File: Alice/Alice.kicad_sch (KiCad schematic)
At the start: 46 parts

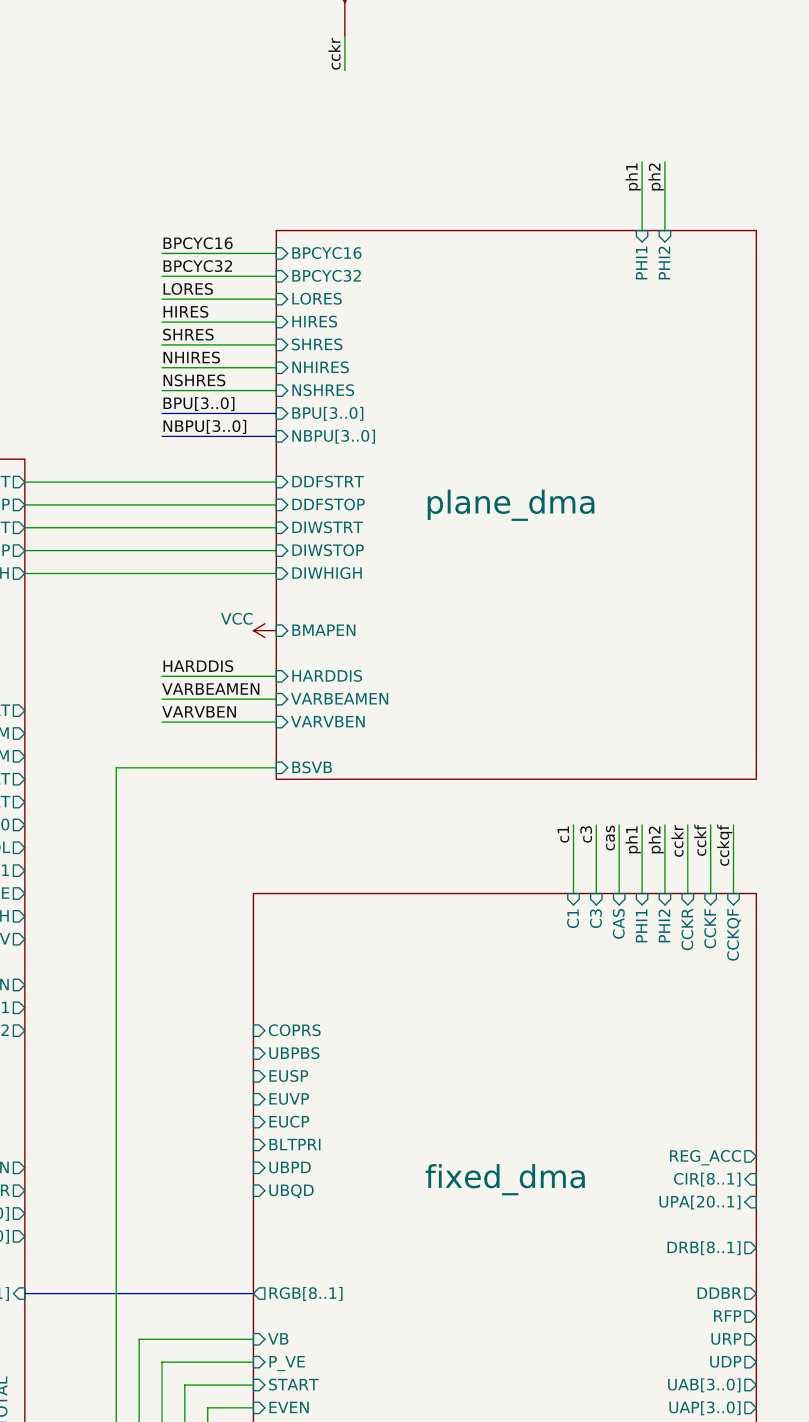
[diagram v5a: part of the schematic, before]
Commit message: Bitplane DMA runs in simulation
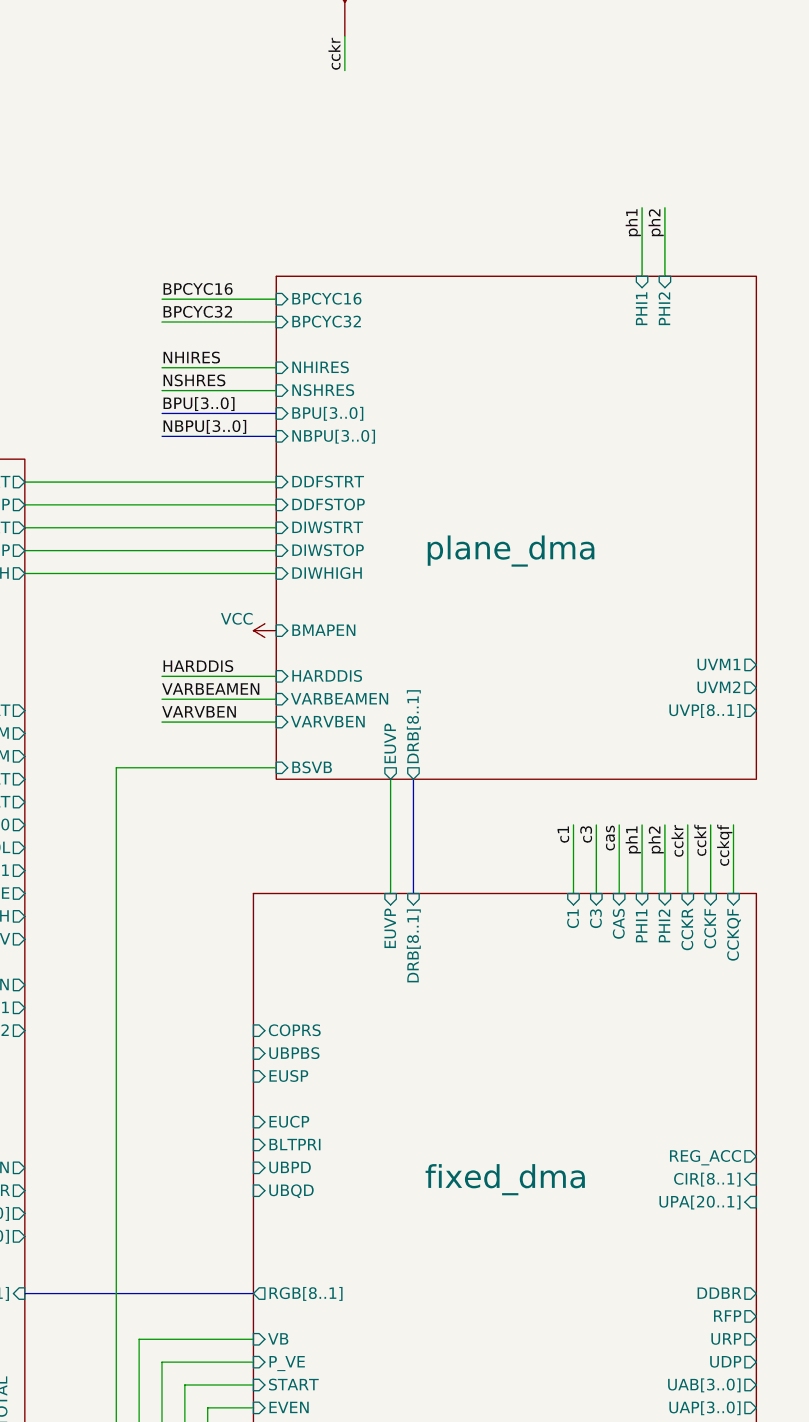
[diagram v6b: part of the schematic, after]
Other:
- sheet plane_dma ports: added DRB[8..1], EUVP, UVM1, UVM2, UVP[8..1]; removed HIRES, LORES, SHRES

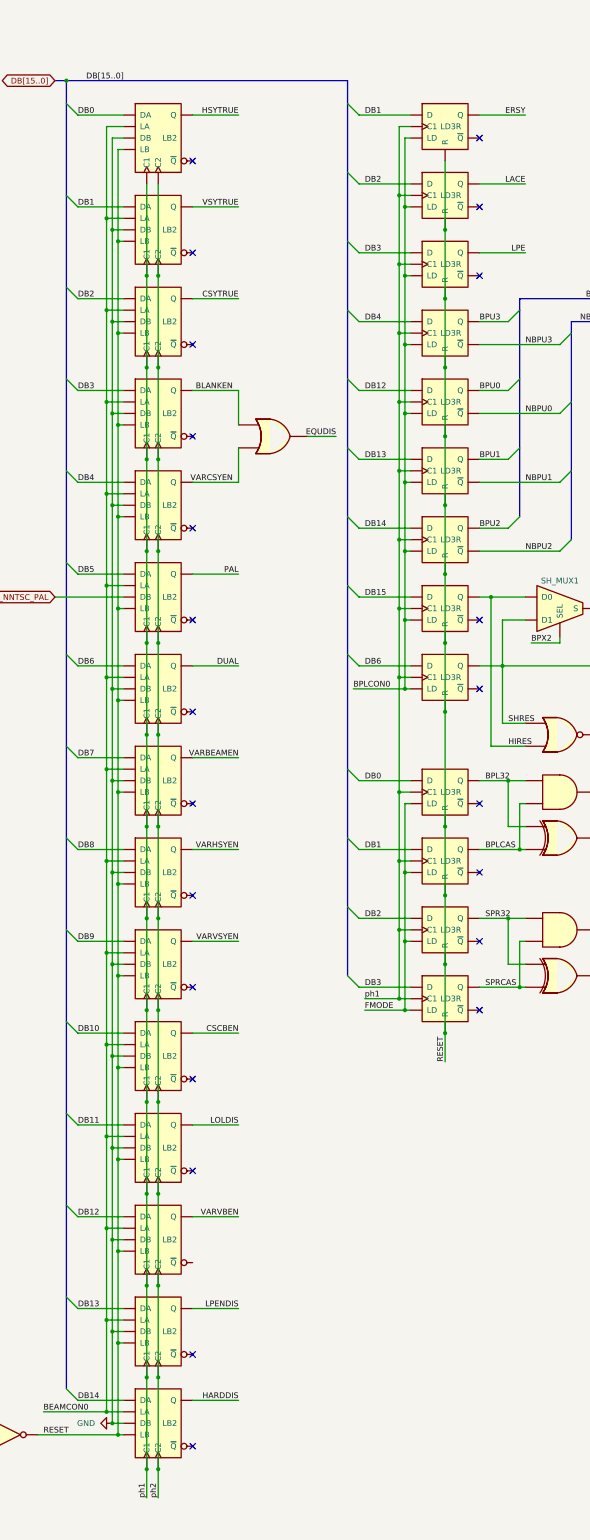
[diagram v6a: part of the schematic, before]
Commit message: Schematics have been annotated
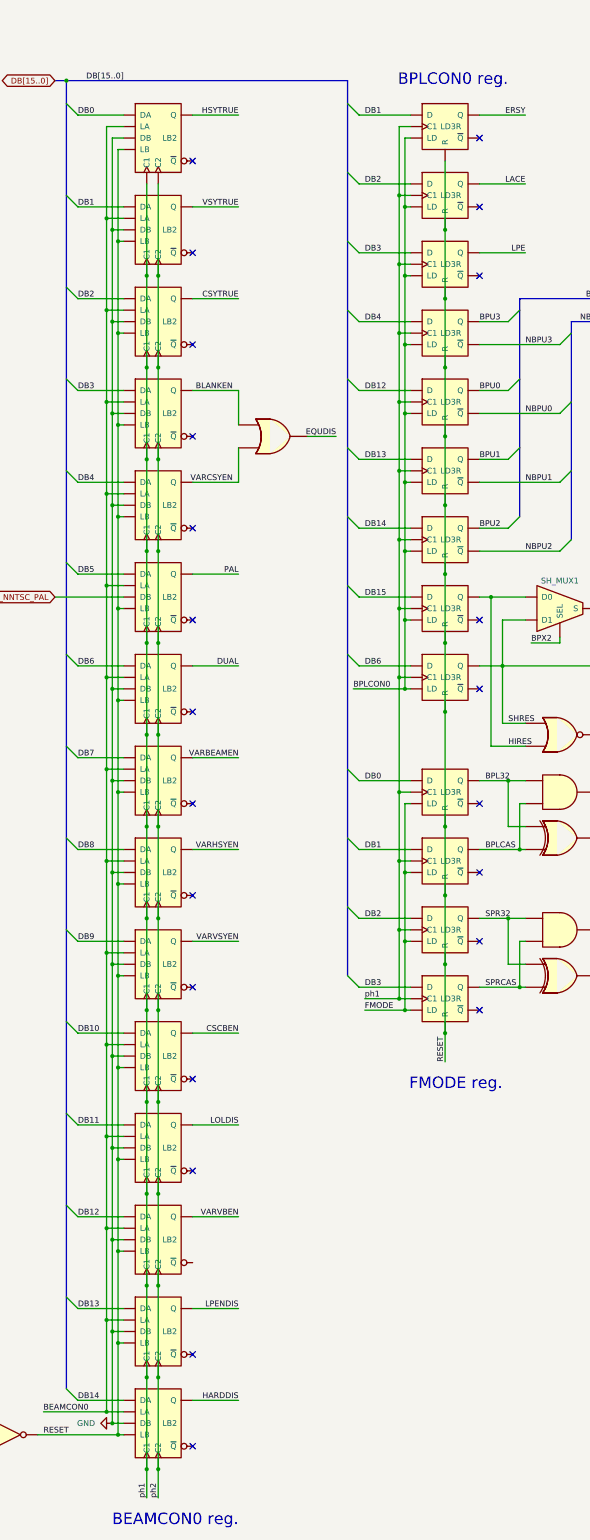
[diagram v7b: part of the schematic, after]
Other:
- note added: "BEAMCON0 reg."
- note added: "BPLCON0 reg."
- note added: "FMODE reg."
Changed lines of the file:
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@@
     (stroke (width 0) (type default) (color 0 0 0 0))
+  )
+  (text "FMODE reg." (at 147.32 287.02 180)
+    (effects (font (size 2.54 2.54)) (justify right bottom))
+  )
+  (text "BPLCON0 reg." (at 148.59 64.77 180)
+    (effects (font (size 2.54 2.54)) (justify right bottom))
+  )
+  (text "BEAMCON0 reg." (at 88.9 383.54 180)
+    (effects (font (size 2.54 2.54)) (justify right bottom))
   )
   (label "CSYTRUE" (at 88.9 111.76 180)

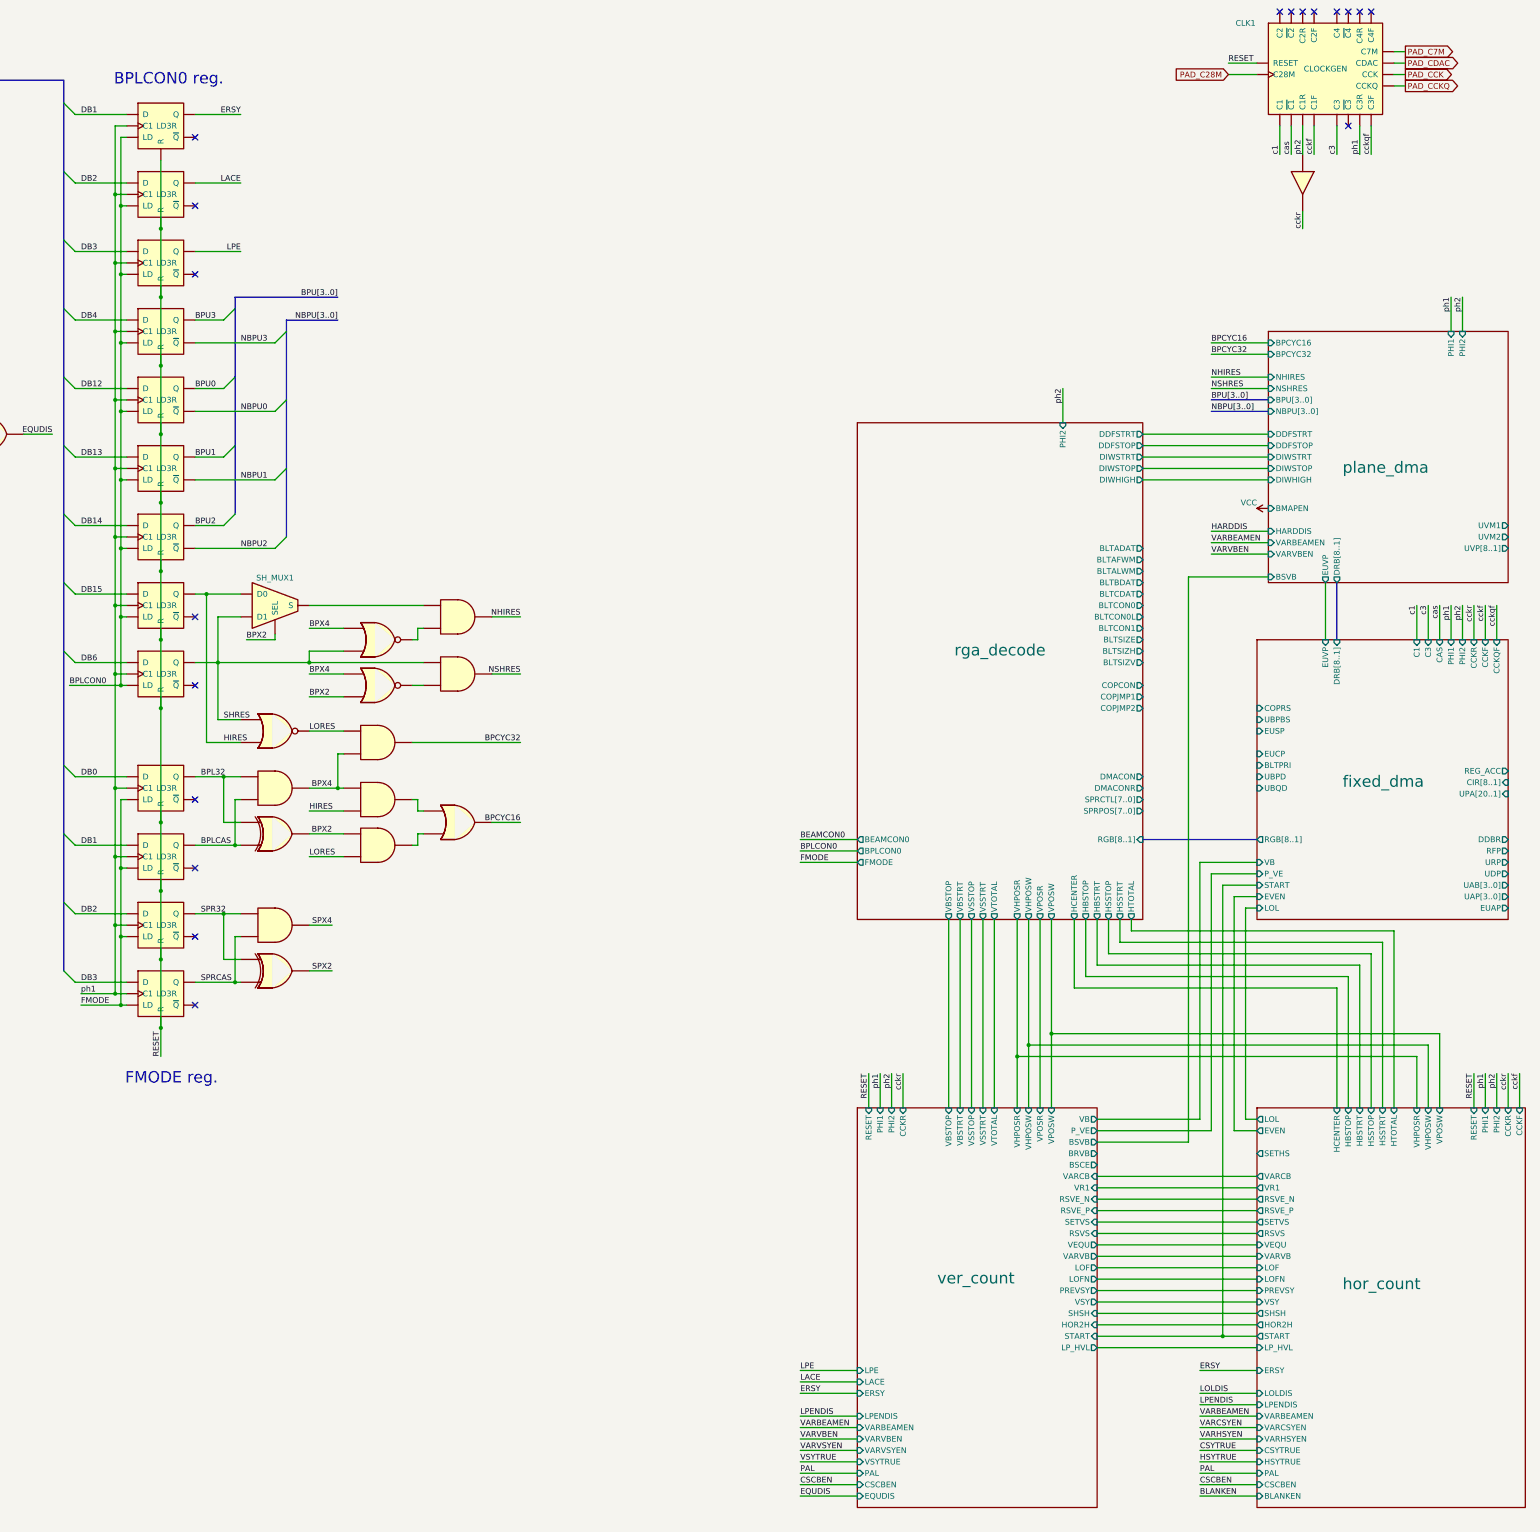
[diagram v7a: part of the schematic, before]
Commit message: Added Copper DMA schematics (WIP)
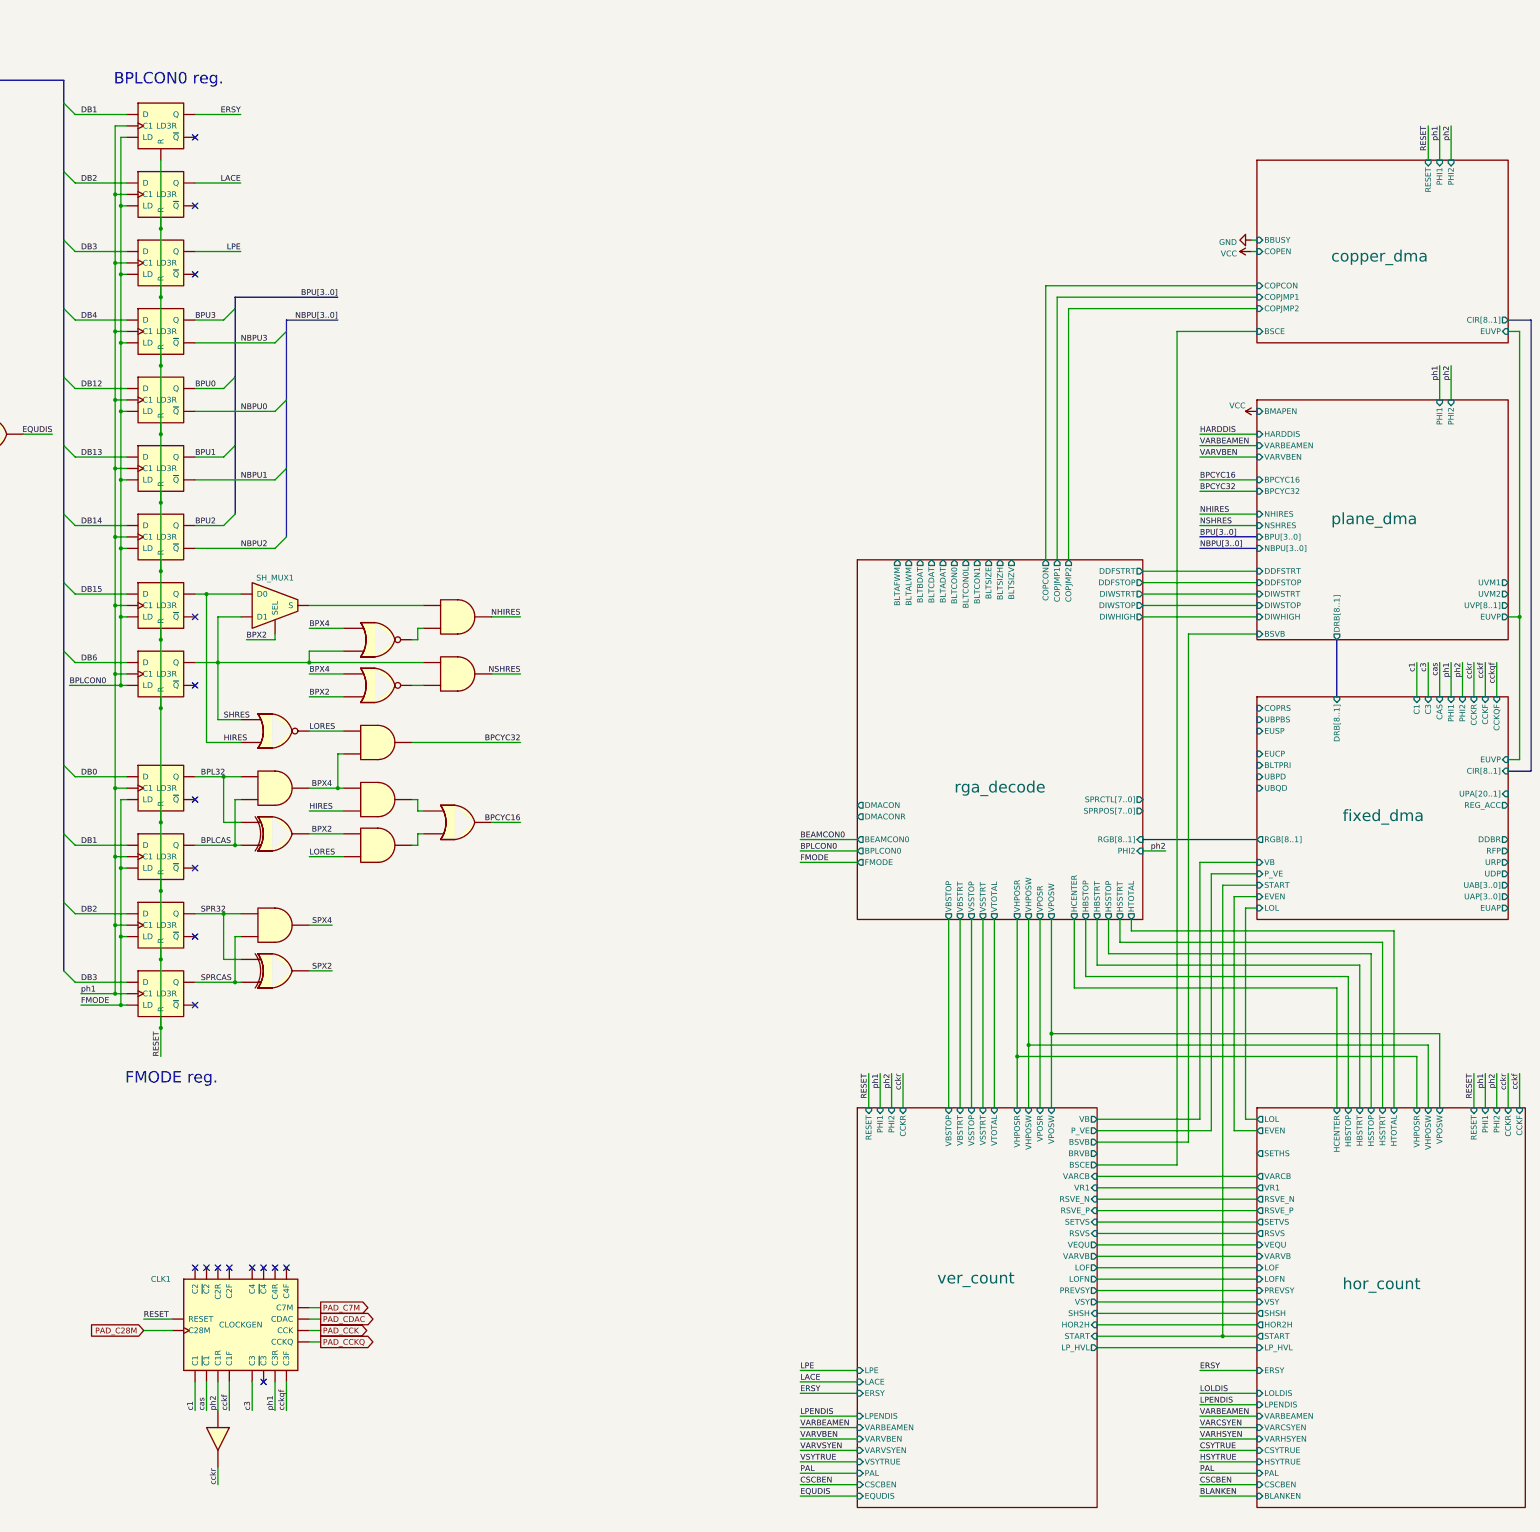
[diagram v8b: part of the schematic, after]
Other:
- added sheet copper_dma (copper_dma.kicad_sch)
- moved on the sheet: CLK1
